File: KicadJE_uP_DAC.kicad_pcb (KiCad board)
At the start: 2 copper layers, 100 x 100 mm, 216 parts, among them J201 CV1, J202 CV2, J203 OUT1, J204 OUT2, J205 IN1, J206 IN2, J301 AVR-ISP-6, J302 UART, J401 CV1, J402 CV2, J403 OUT1, J404 OUT2, J405 OUT3, J406 OUT4, J407 IN1, J408 IN2, J409 I2C, J501 BOOT, J502 UART, J503 USB_B_Micro, P201 Doepfer_Power_16pin, P401 Doepfer_Power_16pin, SW201 SW_SPDT, SW401 SW_SPDT, U201 TL072, U202 MCP4822, U301 ATmega32A-AU, U401 TL072, U402 TL072, U405 MCP4822, U501 AMS1117-3.3, U502 STM32F103C8Tx, Y301 16MHz, Y501 8 MHz

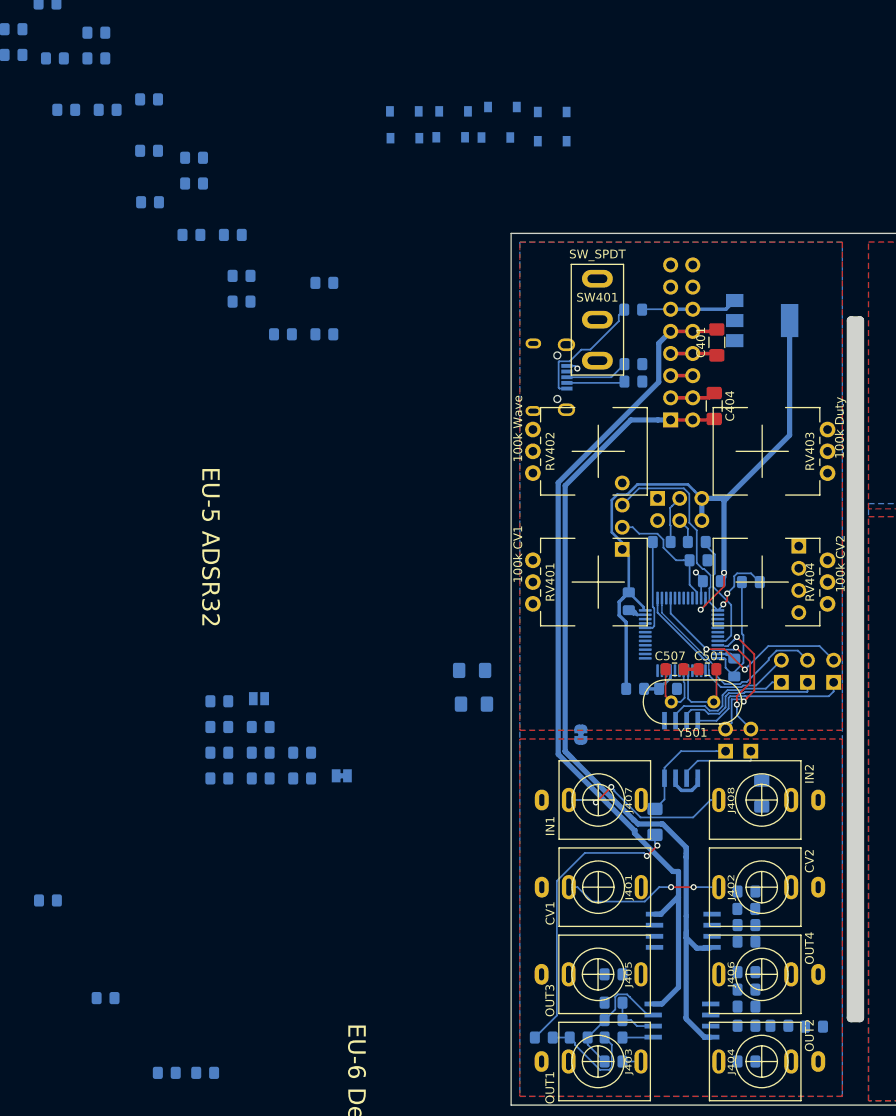
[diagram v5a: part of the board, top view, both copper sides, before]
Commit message: MCP to GNDA and 3.3VA
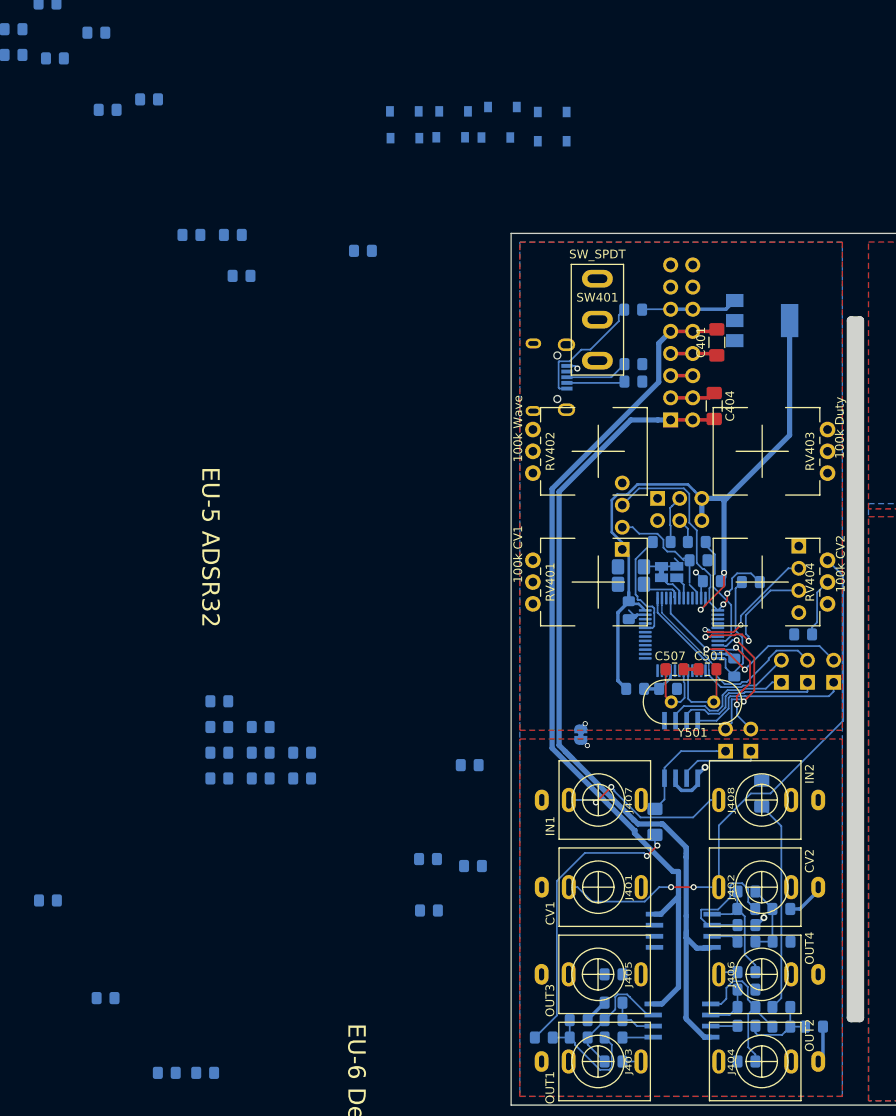
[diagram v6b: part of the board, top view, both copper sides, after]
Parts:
- moved C409 135.7 mm to (84.8, 141.0), turned to 0 degrees
- moved C415 123.4 mm to (57.8, 140.2), turned to 0 degrees
- moved R411 110.0 mm to (81.0, 131.2)
- moved C412 87.3 mm to (40.6, 127.7)
- moved R416 87.3 mm to (45.6, 122.6)
- moved R425 87.3 mm to (40.5, 121.8)
- moved C410 87.3 mm to (81.0, 127.5), turned to 0 degrees
- moved R402 68.1 mm to (83.5, 96.0)
- moved R423 52.2 mm to (45.2, 111.0)
- moved JP402 50.1 mm to (69.0, 88.8), turned to 90 degrees
- moved JP401 43.5 mm to (67.2, 88.8), turned to 90 degrees
- moved C408 23.9 mm to (63.8, 88.2), turned to 0 degrees
- moved C414 20.7 mm to (63.8, 90.2), turned to 0 degrees
- moved R428 15.1 mm to (33.0, 52.0)
- moved R409 4.37 mm to (81.0, 138.8), turned to 0 degrees
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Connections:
- C417 pad 1: +5V -> +3.3VA
- U405 pad 1: +5V -> +3.3VA
- U405 pad 5: GND -> GNDA
- U405 pad 7: GND -> GNDA
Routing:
- net Net-(J401-PadTN): track 18.6 -> 64.1 mm
- net Net-(C407-Pad1): track 0.00 -> 24.4 mm
- net GNDA: track 42.2 -> 62.2 mm, vias 7 -> 10
- net Net-(C405-Pad1): track 0.00 -> 19.3 mm
- net PB7_SDA1: track 0.00 -> 17.2 mm, vias 0 -> 2
- net PB6_SCL1: track 0.00 -> 16.1 mm, vias 0 -> 2
- net Net-(R405-Pad2): track 0.00 -> 15.8 mm
- net Net-(C406-Pad1): track 0.00 -> 13.3 mm
- net Net-(C405-Pad2): track 0.00 -> 9.25 mm
- net Net-(C406-Pad2): track 0.00 -> 8.54 mm
- net Net-(R402-Pad1): track 0.00 -> 6.74 mm
- net Net-(R403-Pad2): track 0.00 -> 5.45 mm
- net PWM_PA8: track 0.00 -> 4.63 mm
- net PWM_PA9: track 0.00 -> 4.56 mm
- net GND: track 79.5 -> 75.7 mm, vias 9 -> 10
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
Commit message: I'll probably have to skip the LED array
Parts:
- moved C416 114.1 mm to (54.5, 128.5)
- moved R424 113.0 mm to (61.8, 132.8), turned to 0 degrees
- moved R418 106.0 mm to (64.2, 108.0)
- moved C417 90.6 mm to (64.2, 106.0)
- moved R415 85.1 mm to (61.8, 128.5), turned to 0 degrees
- moved C402 78.0 mm to (39.2, 76.9)
- moved C403 78.0 mm to (40.0, 88.8)
- moved R401 78.0 mm to (43.9, 85.8)
- moved R417 74.1 mm to (64.2, 104.1)
- moved R435 70.5 mm to (83.6, 82.0), turned to 90 degrees
- moved R436 68.9 mm to (85.6, 82.0), turned to 90 degrees
- moved R426 65.8 mm to (47.4, 109.1)
- moved R427 64.5 mm to (55.4, 58.8), turned to 0 degrees
- moved R425 30.6 mm to (62.2, 100.3), turned to 0 degrees
- moved R428 22.6 mm to (55.4, 55.1), turned to 0 degrees
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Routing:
- net Net-(C408-Pad1): track 0.00 -> 121.9 mm, vias 0 -> 2
- net /KicadJE_STM32F0/STM32F103C8/STM32_PC14: track 0.00 -> 66.1 mm, vias 0 -> 4
- net Net-(C414-Pad1): track 0.00 -> 47.8 mm, vias 0 -> 2
- net Net-(J401-PadT): track 0.00 -> 46.8 mm, vias 0 -> 4
- net Net-(J407-PadT): track 0.00 -> 38.5 mm, vias 0 -> 1
- net /KicadJE_STM32F0/STM32F103C8/STM32_USB_P_PA12: track 0.00 -> 36.2 mm, vias 0 -> 4
- net /KicadJE_STM32F0/STM32F103C8/STM32_USB_N_PA11: track 0.00 -> 36.1 mm, vias 0 -> 4
- net +3V3: track 97.3 -> 131.7 mm, vias 2 -> 3
- net /KicadJE_STM32F0/STM32F103C8/STM32_PC15: track 0.00 -> 21.8 mm, vias 0 -> 4
- net Net-(J407-PadTN): track 20.4 -> 34.8 mm
- net GNDA: track 62.2 -> 75.4 mm, vias 10 -> 14
- net Net-(C412-Pad1): track 0.00 -> 13.2 mm
- net STM32_IN1: track 0.00 -> 11.7 mm
- net Net-(R415-Pad2): track 0.00 -> 11.5 mm
- net Net-(C412-Pad2): track 0.00 -> 8.78 mm
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
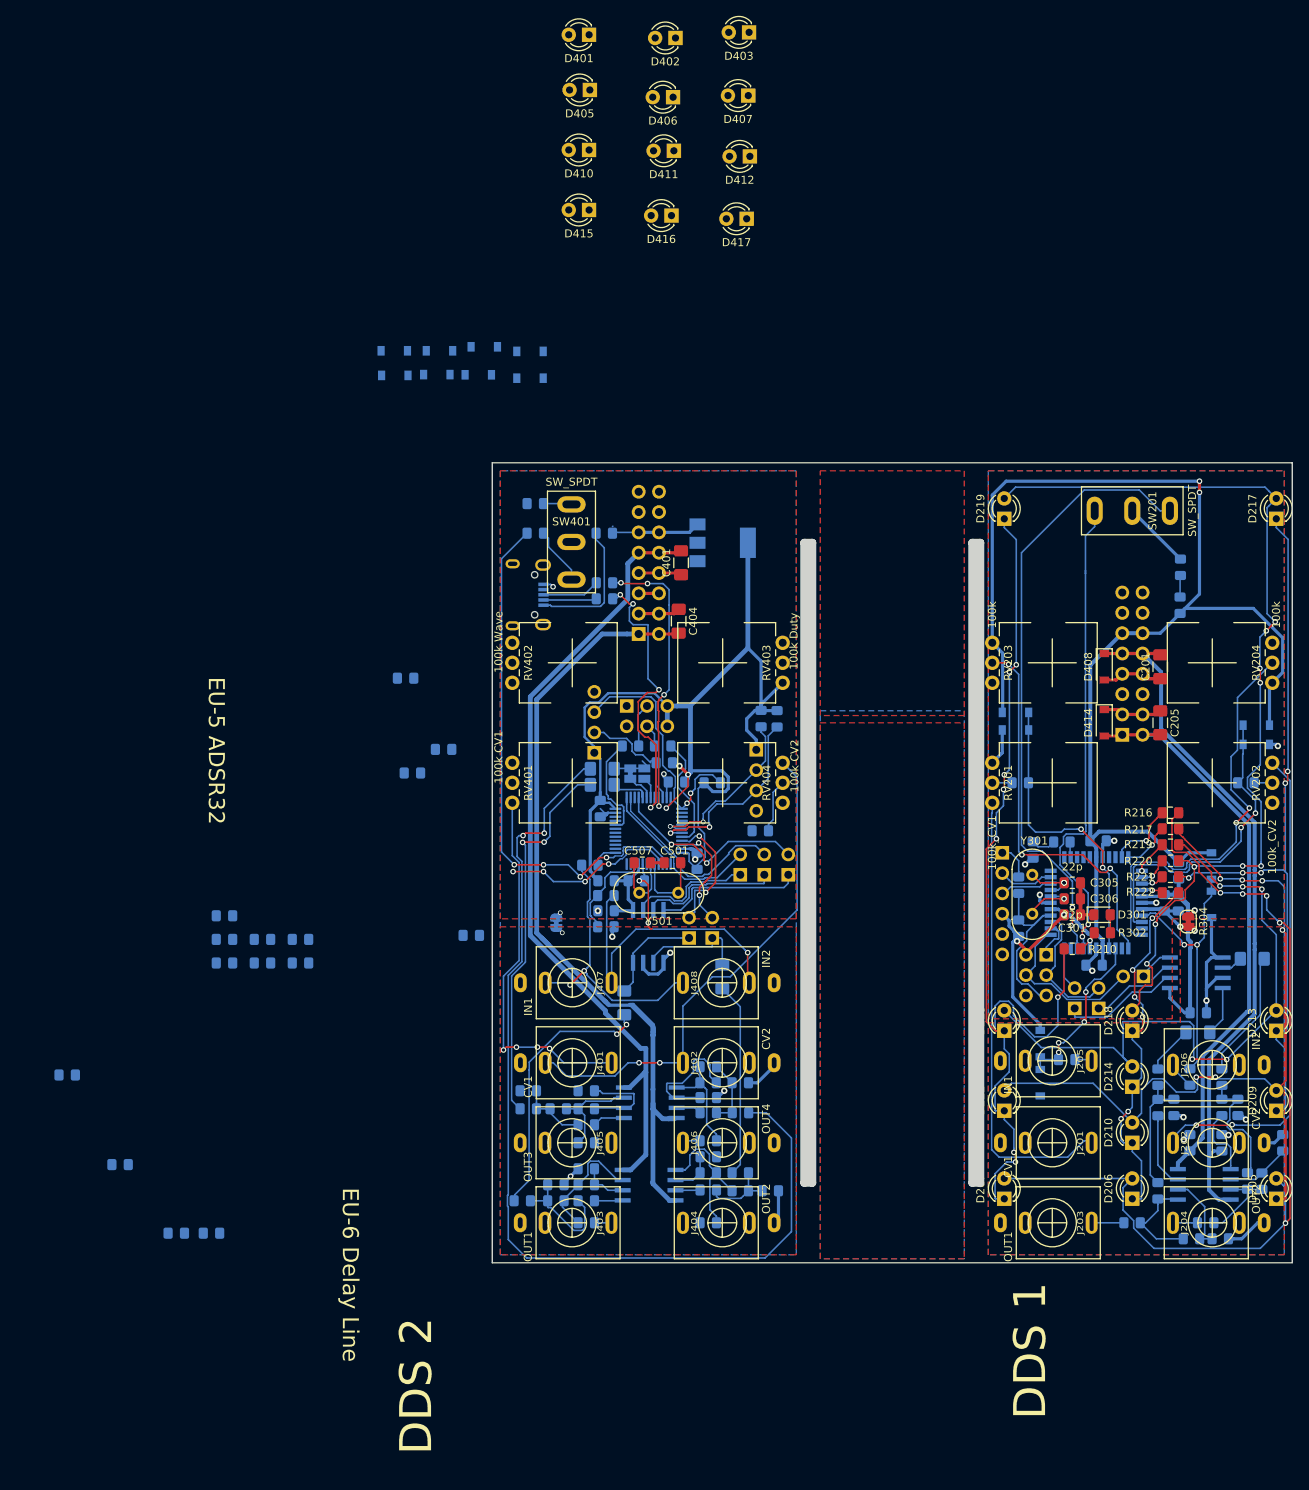
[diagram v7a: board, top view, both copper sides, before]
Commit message: tweaking vias and routing around STM32
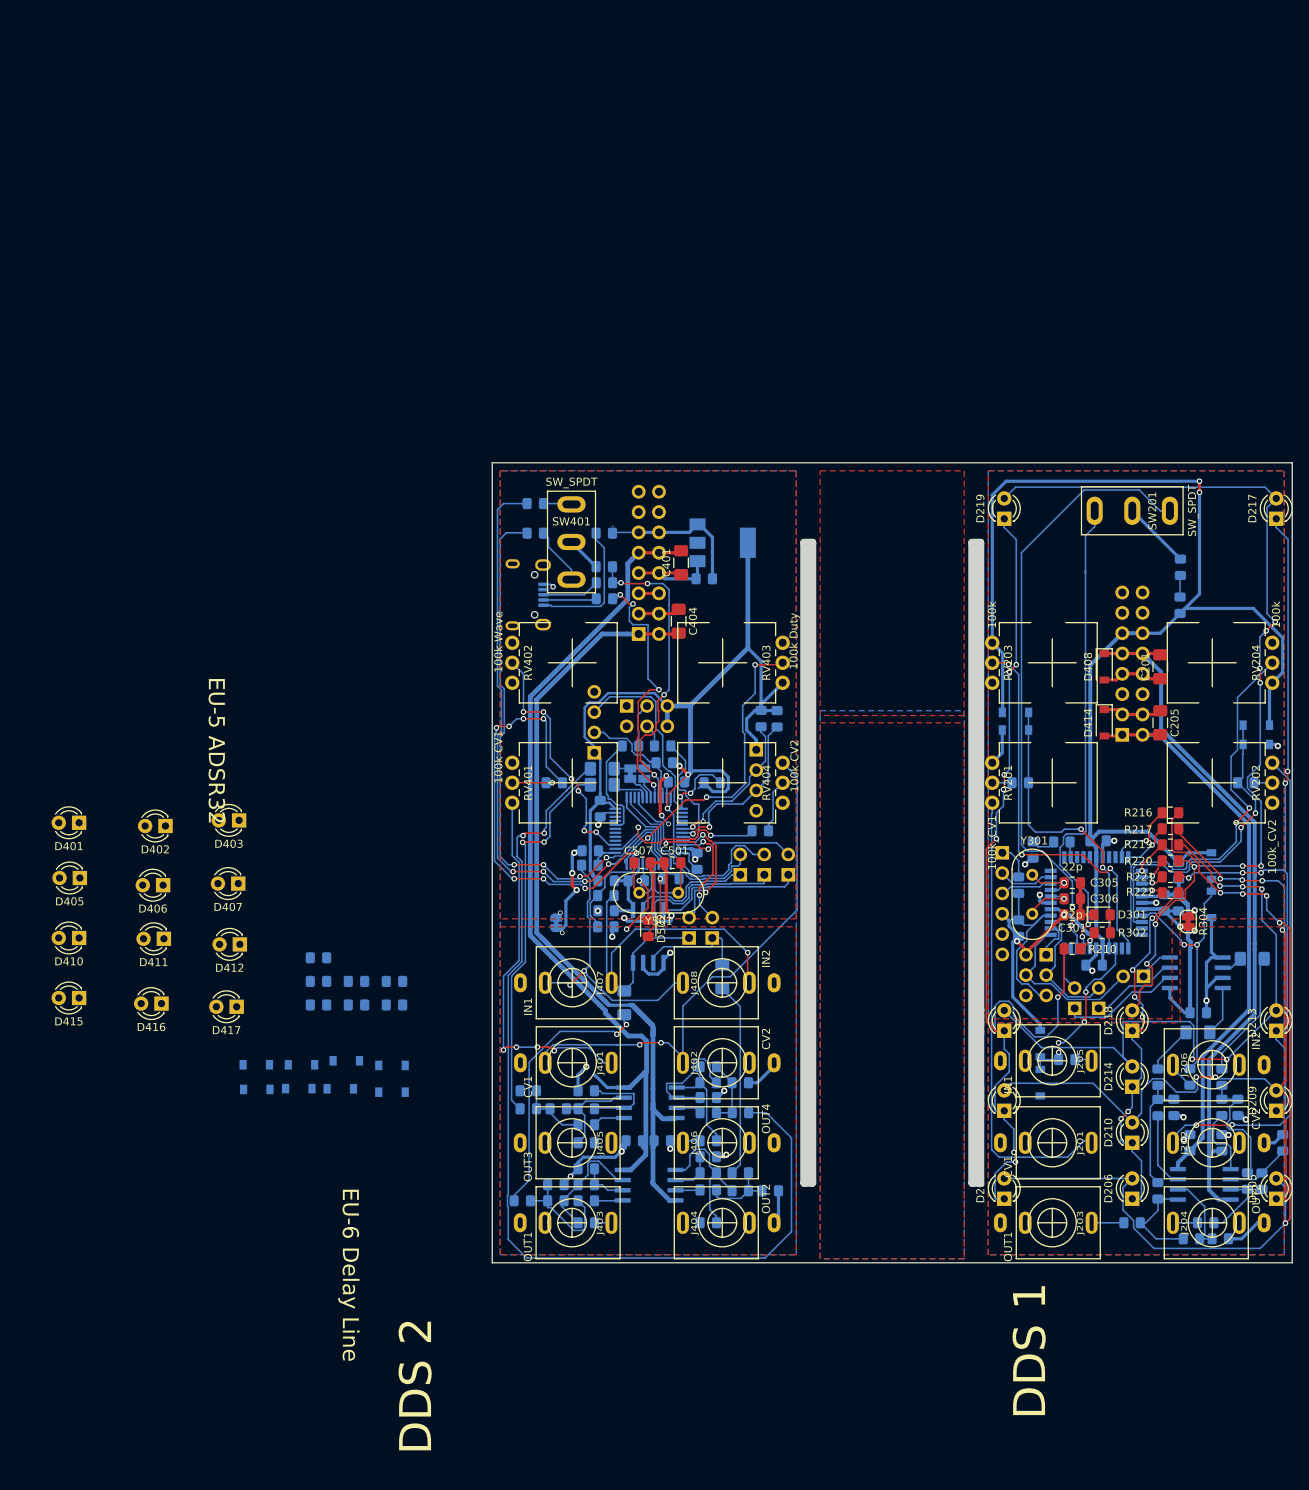
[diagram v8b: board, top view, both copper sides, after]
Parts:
- D502: moved to F.Cu
- moved D401 117.3 mm to (-1.65, 95.0)
- moved D402 117.3 mm to (9.15, 95.4)
- moved D403 117.3 mm to (18.4, 94.7)
- moved D405 117.3 mm to (-1.55, 101.9)
- moved D406 117.3 mm to (8.85, 102.8)
- moved D407 117.3 mm to (18.2, 102.6)
- moved D410 117.3 mm to (-1.65, 109.4)
- moved D411 117.3 mm to (8.95, 109.5)
- moved D412 117.3 mm to (18.4, 110.2)
- moved D415 117.3 mm to (-1.65, 116.9)
- moved D416 117.3 mm to (8.65, 117.6)
- moved D417 117.3 mm to (18.1, 118.0)
- moved C502 103.4 mm to (76.5, 64.5), turned to 0 degrees
- moved R508 92.4 mm to (64.0, 63.0), turned to 0 degrees
- moved D404 90.9 mm to (31.0, 128.2)
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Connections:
- D403 pad 1: Net-(D403-Pad1) -> PA15_C2
- D407 pad 1: Net-(D403-Pad1) -> PA15_C2
- D412 pad 1: Net-(D403-Pad1) -> PA15_C2
- D417 pad 1: Net-(D403-Pad1) -> PA15_C2
- R429 pad 1: /KicadJE_STM32F0/STM32F103C8/STM32_PB0 -> (no net)
- R430 pad 1: /KicadJE_STM32F0/STM32F103C8/STM32_PB1 -> (no net)
- R431 pad 1: /KicadJE_STM32F0/STM32F103C8/STM32_boot1_PB2 -> (no net)
- R432 pad 1: /KicadJE_STM32F0/STM32F103C8/STM32_PB3 -> (no net)
- R433 pad 1: /KicadJE_STM32F0/STM32F103C8/STM32_PB4 -> (no net)
- R434 pad 1: /KicadJE_STM32F0/STM32F103C8/STM32_PB5 -> (no net)
- R437 pad 1: /KicadJE_STM32F0/STM32F103C8/STM32_PA15 -> (no net)
- R437 pad 2: PB5_C1 -> PA15_C2
- U502 pad 18: /KicadJE_STM32F0/STM32F103C8/STM32_PB0 -> (no net)
- U502 pad 19: /KicadJE_STM32F0/STM32F103C8/STM32_PB1 -> (no net)
- U502 pad 38: /KicadJE_STM32F0/STM32F103C8/STM32_PA15 -> (no net)
- U502 pad 39: /KicadJE_STM32F0/STM32F103C8/STM32_PB3 -> (no net)
- U502 pad 40: /KicadJE_STM32F0/STM32F103C8/STM32_PB4 -> (no net)
- U502 pad 41: /KicadJE_STM32F0/STM32F103C8/STM32_PB5 -> (no net)
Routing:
- net STM32_CV1: track 0.00 -> 54.8 mm, vias 0 -> 8
- net /KicadJE_STM32F0/STM32F103C8/STM32_PC15: track 21.8 -> 75.7 mm
- net STM32_Duty: track 0.00 -> 38.9 mm, vias 0 -> 3
- net GND: track 76.8 -> 110.3 mm, vias 12 -> 17
- net STM32_Wave: track 0.00 -> 31.0 mm, vias 0 -> 6
- net GNDA: track 75.4 -> 104.4 mm, vias 14 -> 21
- net STM32_CV2: track 0.00 -> 21.5 mm, vias 0 -> 2
- net Net-(D502-Pad2): track 0.00 -> 8.33 mm, vias 0 -> 1
- net +5V: track 212.3 -> 220.0 mm
- net +12V: track 187.0 -> 193.9 mm
- net /KicadJE_STM32F0/STM32F103C8/STM32_PC14: track 66.1 -> 71.9 mm
- net Net-(R401-Pad1): track 0.00 -> 5.77 mm, vias 0 -> 1
- net /KicadJE_STM32F0/STM32F103C8/STM32_USB_N_PA11: track 36.1 -> 32.9 mm
- net /KicadJE_STM32F0/STM32F103C8/STM32_LED_PC13: track 0.00 -> 2.80 mm
- net PB7_SDA1: track 24.6 -> 22.0 mm
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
